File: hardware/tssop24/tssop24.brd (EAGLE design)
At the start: 17.8 x 30.5 mm, 3 parts, among them U1 CML-MICRO_CMX589AE2

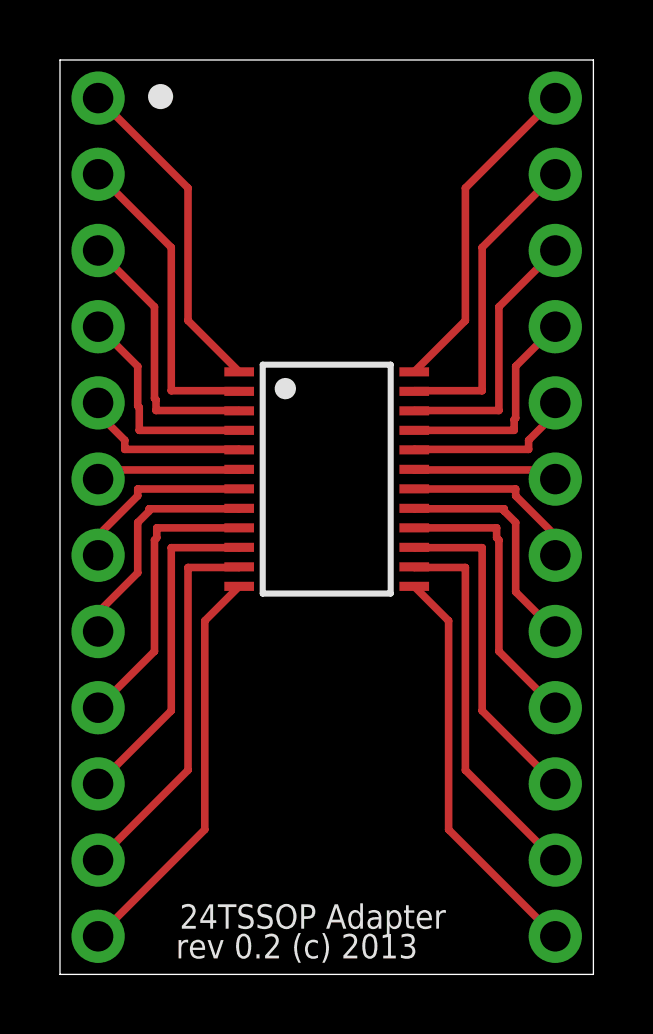
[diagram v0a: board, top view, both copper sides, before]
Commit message: 
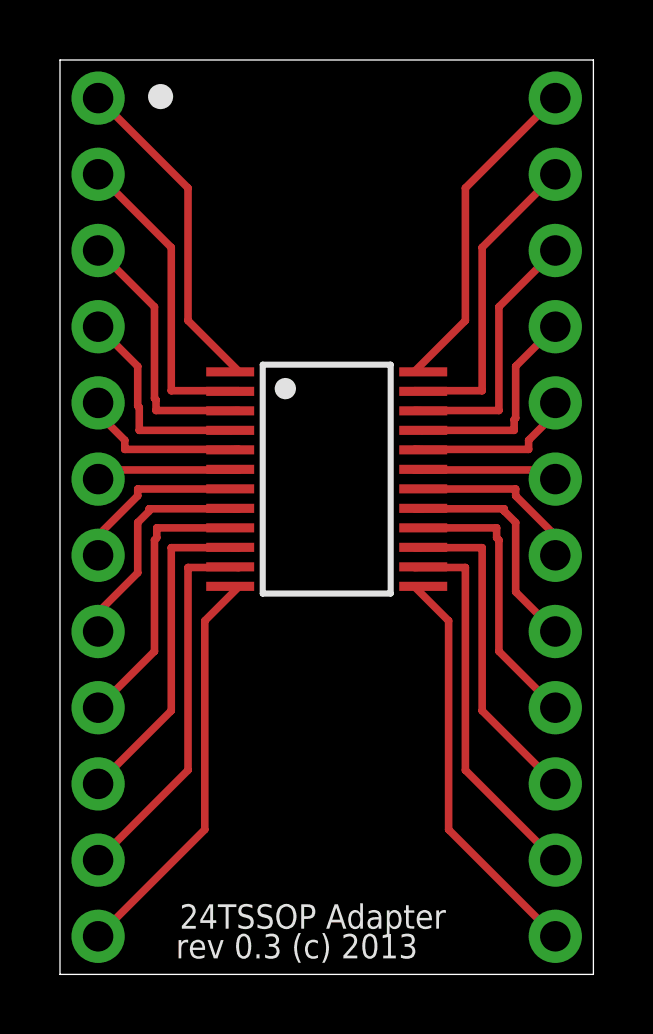
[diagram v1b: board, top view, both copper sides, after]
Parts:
- U1: device 12_dollar:AIS_MK2_CML-MICRO_TSSOP24 -> mylibrary:AIS_MK2_CML-MICRO_TSSOP24
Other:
- board text added: "rev 0.3 (c) 2013"
- board text removed: "rev 0.2 (c) 2013"
